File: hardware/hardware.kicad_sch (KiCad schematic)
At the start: 25 parts, among them J1 Conn_02x03_Odd_Even, U1 CH32V003FxPx

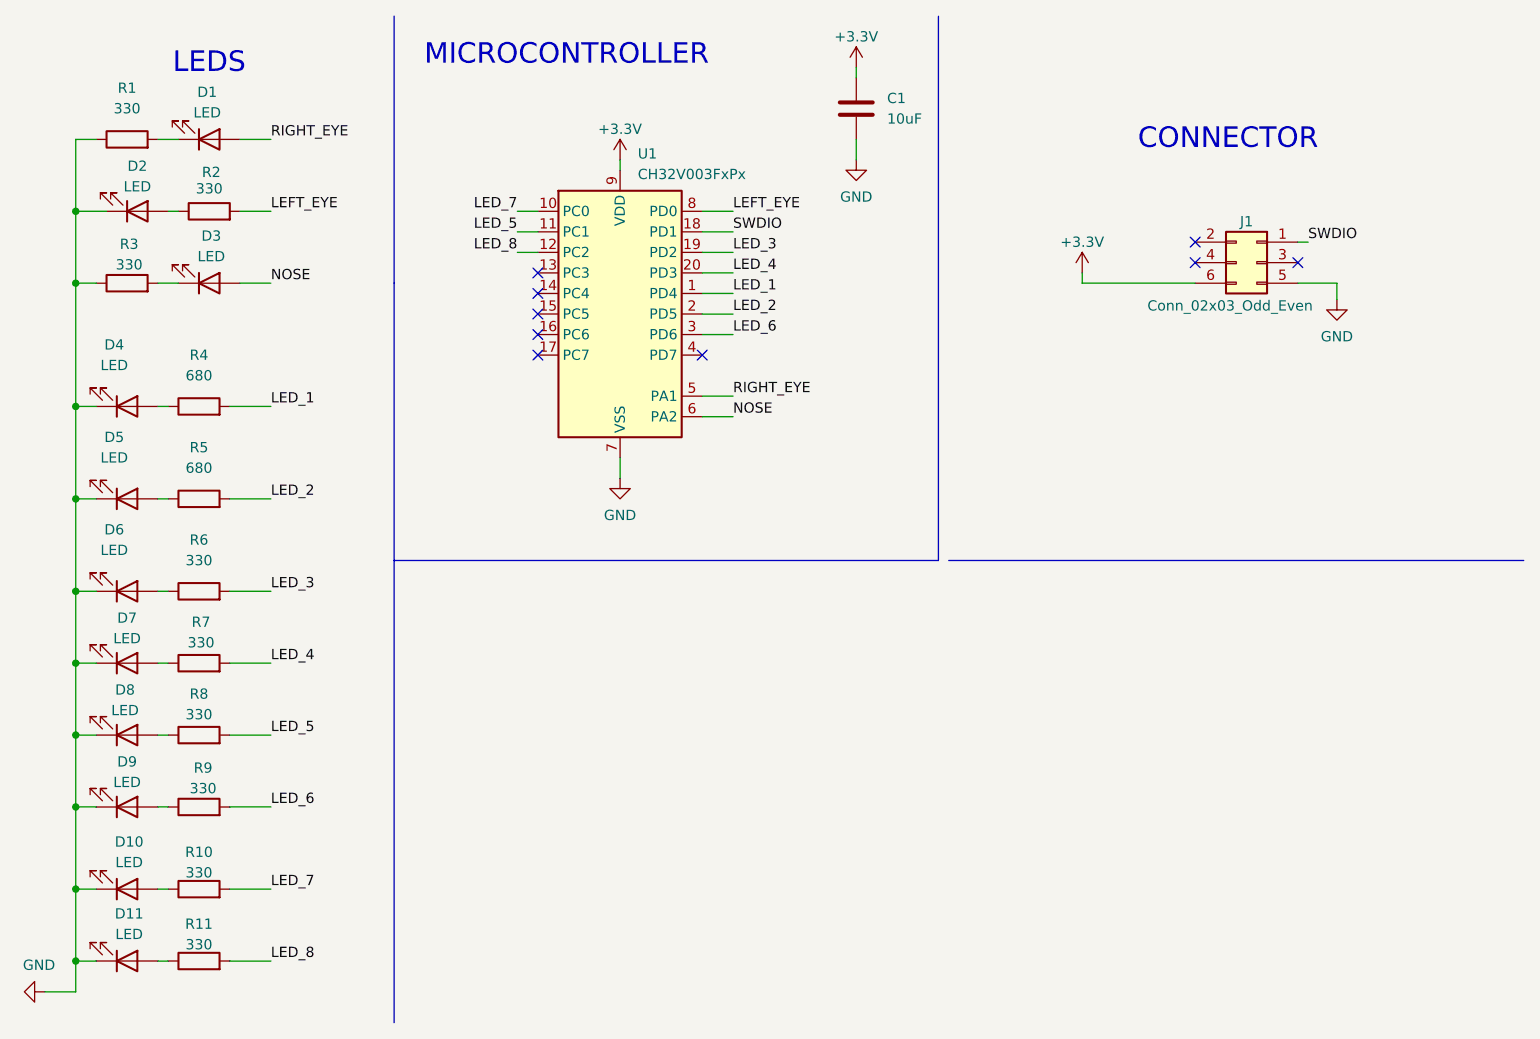
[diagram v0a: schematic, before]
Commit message: feat: change routes and components place
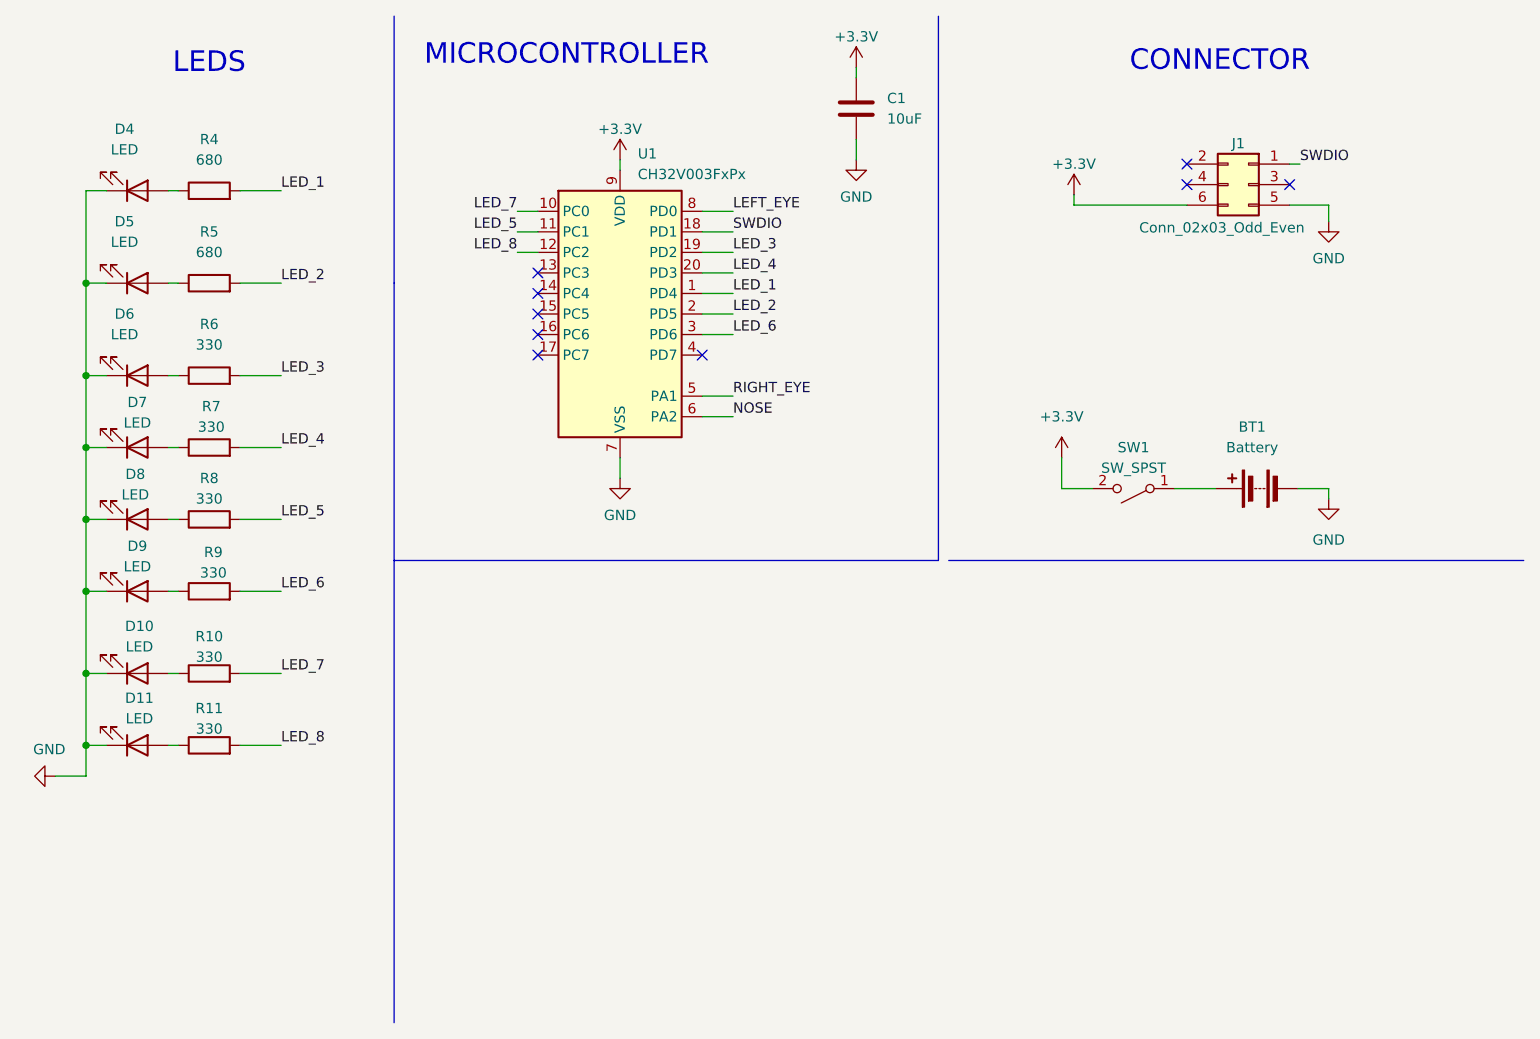
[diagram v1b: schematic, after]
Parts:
- removed D1, D2, D3: LED, footprints:LYT77K-K2M1, symbol Device:LED
- removed R1, R2, R3: 330, Resistor_SMD:R_0402_1005Metric_Pad0.72x0.64mm_HandSolder, symbol Device:R
- added BT1: Battery, footprints:BAT-HLD-001, symbol Device:Battery
- added SW1: SW_SPST, Button_Switch_SMD:SW_SPDT_PCM12, symbol Switch:SW_SPST
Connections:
- net +3.3V: now also SW1.2 (B)
- net GND: now also BT1.1 (-)
- new net: BT1.2 (+), SW1.1 (A)
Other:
- moved on the sheet: D10, D11, D4, D5, D6, D7, D8, D9, J1, R10, R11, R4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

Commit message: feat: add routes and update hardware
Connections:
- net RIGHT_EYE is gone; now on net LED_2: U1.5 (PA1)
- net LED_1: now also U1.4 (PD7); no longer U1.1 (PD4)
- net LED_2: no longer U1.2 (PD5)
- net LED_3: now also U1.3 (PD6); no longer U1.19 (PD2)
- net LED_4: now also U1.10 (PC0); no longer U1.20 (PD3)
- net LED_5: now also U1.2 (PD5); no longer U1.11 (PC1)
- net LED_6: now also U1.17 (PC7); no longer U1.3 (PD6)
- net LED_7: now also U1.19 (PD2); no longer U1.10 (PC0)
- net LED_8: now also U1.1 (PD4); no longer U1.12 (PC2)
- net LEFT_EYE: no longer names the net of U1.8 (PD0)
- net NOSE: no longer names the net of U1.6 (PA2)
- no-connect marks 9 -> 10
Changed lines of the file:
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@@
 	)
 	(no_connect
-		(at 96.52 53.34)
+		(at 76.2 40.64)
 	)
 	(no_connect
@@
 	)
 	(no_connect
-		(at 76.2 53.34)
+		(at 76.2 38.1)
 	)
 	(no_connect
@@
 	)
 	(no_connect
+		(at 96.52 43.18)
+	)
+	(no_connect
 		(at 156.464 29.718)
 	)
@@
 	(wire
 		(pts
+			(xy 96.52 58.42) (xy 100.33 58.42)
+		)
+		(stroke
+			(width 0)
+			(type default)
+		)
+	)
+	(wire
+		(pts
+			(xy 96.52 53.34) (xy 100.33 53.34)
+		)
+		(stroke
+			(width 0)
+			(type default)
+		)
+	)
+	(wire
+		(pts
 			(xy 39.37 73.66) (xy 44.45 73.66)
 		)
@@
 		)
 	)
-	(wire
-		(pts
-			(xy 96.52 58.42) (xy 100.33 58.42)
-		)
-		(stroke
-			(width 0)
-			(type default)
-		)
-	)
 	(polyline
 		(pts
@@
 	(wire
 		(pts
+			(xy 73.66 35.56) (xy 76.2 35.56)
+		)
+		(stroke
+			(width 0)
+			(type default)
+		)
+	)
+	(wire
+		(pts
 			(xy 142.494 33.528) (xy 142.494 34.798)
 		)
@@
 	(wire
 		(pts
-			(xy 96.52 60.96) (xy 100.33 60.96)
-		)
-		(stroke
-			(width 0)
-			(type default)
-		)
-	)
-	(wire
-		(pts
-			(xy 73.66 35.56) (xy 76.2 35.56)
-		)
-		(stroke
-			(width 0)
-			(type default)
-		)
-	)
-	(wire
-		(pts
 			(xy 31.75 73.66) (xy 30.48 73.66)
 		)
@@
 	(wire
 		(pts
+			(xy 73.66 53.34) (xy 76.2 53.34)
+		)
+		(stroke
+			(width 0)
+			(type default)
+		)
+	)
+	(wire
+		(pts
 			(xy 20.32 92.71) (xy 20.32 101.6)
 		)
@@
 	(wire
 		(pts
-			(xy 96.52 43.18) (xy 100.33 43.18)
-		)
-		(stroke
-			(width 0)
-			(type default)
-		)
-	)
-	(wire
-		(pts
 			(xy 39.37 82.55) (xy 44.45 82.55)
 		)
@@
 	(wire
 		(pts
-			(xy 73.66 40.64) (xy 76.2 40.64)
-		)
-		(stroke
-			(width 0)
-			(type default)
-		)
-	)
-	(wire
-		(pts
-			(xy 73.66 38.1) (xy 76.2 38.1)
-		)
-		(stroke
-			(width 0)
-			(type default)
-		)
-	)
-	(wire
-		(pts
 			(xy 173.99 71.12) (xy 173.99 69.85)
 		)
@@
 		(pts
 			(xy 20.32 55.88) (xy 22.86 55.88)
-		)
-		(stroke
-			(width 0)
-			(type default)
-		)
-	)
-	(wire
-		(pts
-			(xy 100.33 35.56) (xy 96.52 35.56)
 		)
 		(stroke
@@
 	)
 	(label "LED_3"
-		(at 100.33 40.64 0)
+		(at 100.33 50.8 0)
 		(effects
 			(font
@@
 	)
 	(label "LED_5"
-		(at 73.66 38.1 180)
-		(effects
-			(font
-				(size 1.27 1.27)
-			)
-			(justify right bottom)
+		(at 100.33 48.26 0)
+		(effects
+			(font
+				(size 1.27 1.27)
+			)
+			(justify left bottom)
 		)
 	)
@@
 	)
 	(label "LED_6"
-		(at 100.33 50.8 0)
-		(effects
-			(font
-				(size 1.27 1.27)
-			)
-			(justify left bottom)
+		(at 73.66 53.34 180)
+		(effects
+			(font
+				(size 1.27 1.27)
+			)
+			(justify right bottom)
 		)
 	)
 	(label "LED_2"
-		(at 100.33 48.26 0)
+		(at 100.33 58.42 0)
 		(effects
 			(font
@@
 	)
 	(label "LED_7"
-		(at 73.66 35.56 180)
-		(effects
-			(font
-				(size 1.27 1.27)
-			)
-			(justify right bottom)
+		(at 100.33 40.64 0)
+		(effects
+			(font
+				(size 1.27 1.27)
+			)
+			(justify left bottom)
 		)
 	)
@@
 	)
 	(label "LED_4"
-		(at 100.33 43.18 0)
-		(effects
-			(font
-				(size 1.27 1.27)
-			)
-			(justify left bottom)
-		)
-	)
-	(label "LEFT_EYE"
-		(at 100.33 35.56 0)
-		(effects
-			(font
-				(size 1.27 1.27)
-			)
-			(justify left bottom)
+		(at 73.66 35.56 180)
+		(effects
+			(font
+				(size 1.27 1.27)
+			)
+			(justify right bottom)
 		)
 	)
@@
 		)
 	)
-	(label "NOSE"
-		(at 100.33 60.96 0)
-		(effects
-			(font
-				(size 1.27 1.27)
-			)
-			(justify left bottom)
-		)
-	)
 	(label "LED_1"
-		(at 100.33 45.72 0)
+		(at 100.33 53.34 0)
 		(effects
 			(font
@@
 	)
 	(label "LED_8"
-		(at 73.66 40.64 180)
-		(effects
-			(font
-				(size 1.27 1.27)
-			)
-			(justify right bottom)
-		)
-	)
-	(label "RIGHT_EYE"
-		(at 100.33 58.42 0)
-		(effects
-			(font
+		(at 100.33 45.72 0)
+		(effects
+			(font
